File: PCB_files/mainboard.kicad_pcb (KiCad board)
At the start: 2 copper layers, 45 parts, among them J1 Conn_01x01_Male, J2 Conn_01x01_Male, J3 Conn_01x01_Male, J4 Conn_01x20, J5 Conn_01x20, J6 Conn_01x06_Male, U1 IFX007TAUMA1, U2 IFX007TAUMA1, U3 IFX007TAUMA1, U4 LM2931-5.0_SO8

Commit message: Started routing components
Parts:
- C1, C2, C3, C4, C5, C6: footprint Capacitor_SMD:C_0805_2012Metric -> Capacitor_SMD:C_0603_1608Metric_Pad1.05x0.95mm_HandSolder; moved to B.Cu
- C14, C15: moved to B.Cu
- R1, R2, R3, R4, R5, R6, R9: footprint Resistor_SMD:R_0805_2012Metric -> Resistor_SMD:R_0603_1608Metric_Pad1.05x0.95mm_HandSolder; moved to B.Cu
- R10, R11, R12, R13, R14, R7, R8: footprint Resistor_SMD:R_0805_2012Metric -> Resistor_SMD:R_0603_1608Metric_Pad1.05x0.95mm_HandSolder
- moved R9 67.4 mm to (192.3, 94.1), turned to 270 degrees
- moved C2 67.2 mm to (178.9, 76.1), turned to 180 degrees
- moved C7 64.1 mm to (198.1, 93.4), turned to 180 degrees
- moved C8 59.4 mm to (198.5, 107.1)
- moved C11 58.2 mm to (187.7, 94.1), turned to 90 degrees
- moved R2 49.0 mm to (177.2, 80.2), turned to 180 degrees
- moved C12 47.4 mm to (188.7, 105.4), turned to 180 degrees
- moved C4 47.2 mm to (168.0, 99.1), turned to 90 degrees
- moved R5 46.9 mm to (143.8, 99.9), turned to 90 degrees
- moved C16 46.2 mm to (189.2, 101.9), turned to 90 degrees
- moved C14 42.5 mm to (162.3, 96.4), turned to 90 degrees
- moved R6 37.0 mm to (140.8, 101.2), turned to 90 degrees
- moved C3 35.8 mm to (162.9, 99.9), turned to 90 degrees
- moved C9 32.5 mm to (137.9, 96.1), turned to 90 degrees
- moved R4 31.5 mm to (170.4, 99.1), turned to 90 degrees
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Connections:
- net Net-(C1-Pad1) renamed /sr1
- net Net-(C3-Pad1) renamed /sr2
- net Net-(C5-Pad1) renamed /sr3
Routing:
- net GND: track 107.8 -> 163.3 mm, vias 0 -> 3
- net +BATT: track 96.4 -> 129.7 mm, vias 0 -> 1
- net Net-(C2-Pad1): track 0.00 -> 30.8 mm, vias 0 -> 2
- net Net-(C7-Pad1): track 0.00 -> 28.2 mm
- net Net-(J4-Pad5): track 0.00 -> 27.6 mm, vias 0 -> 1
- net Net-(C11-Pad1): track 0.00 -> 25.7 mm
- net Net-(C14-Pad1): track 0.00 -> 22.8 mm, vias 0 -> 1
- net /sr1: track 0.00 -> 14.8 mm, vias 0 -> 1
- net Net-(C6-Pad1): track 0.00 -> 8.27 mm, vias 0 -> 1
- net Net-(R9-Pad2): track 0.00 -> 8.05 mm, vias 0 -> 1
- net Net-(C4-Pad1): track 0.00 -> 7.55 mm, vias 0 -> 1
- net /sr3: track 0.00 -> 5.66 mm, vias 0 -> 1
- net /sr2: track 0.00 -> 4.84 mm, vias 0 -> 1

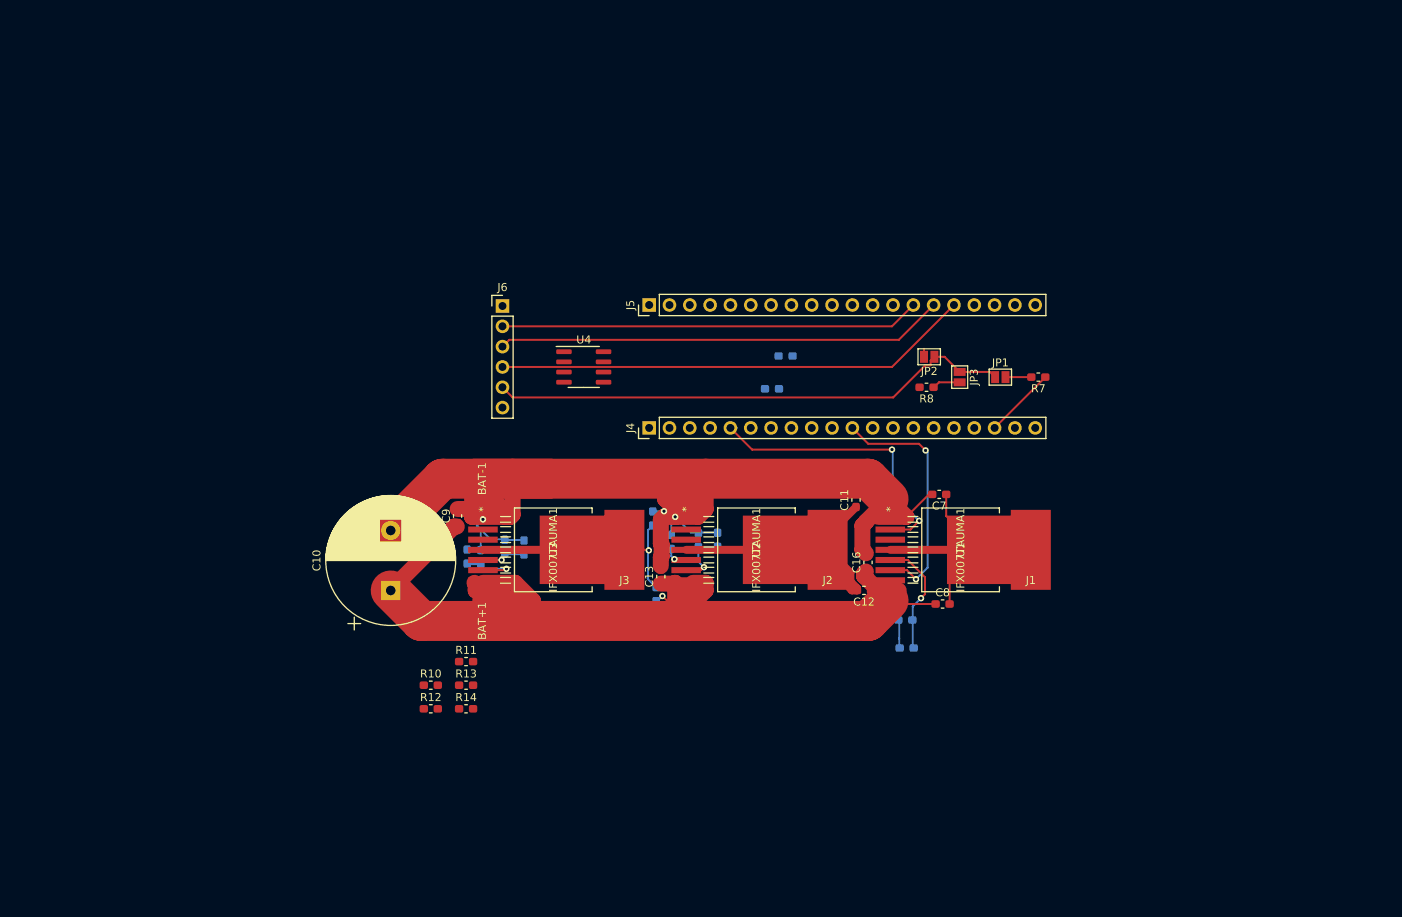
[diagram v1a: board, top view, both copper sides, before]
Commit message: Finished routing and added footprint file for driver chip
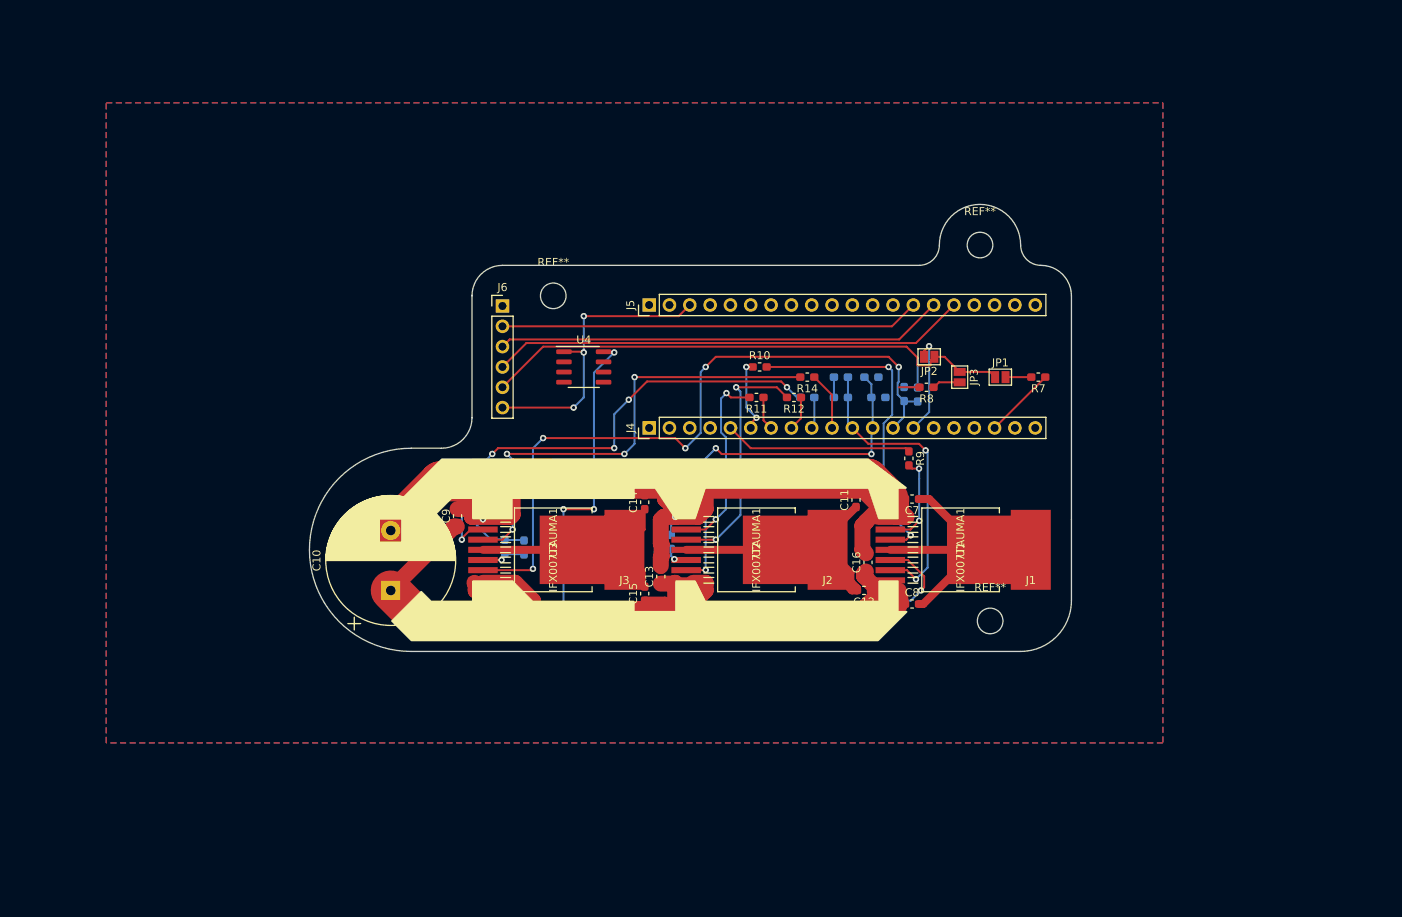
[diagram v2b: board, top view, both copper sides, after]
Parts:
- added REF**: MountingHole_3.2mm_M3, MountingHole:MountingHole_3.2mm_M3, F.Cu at (203.2, 62.2)
- added REF**: MountingHole_3.2mm_M3, MountingHole:MountingHole_3.2mm_M3, F.Cu at (149.9, 68.6)
- added REF**: MountingHole_3.2mm_M3, MountingHole:MountingHole_3.2mm_M3, F.Cu at (204.5, 109.2)
- C14, C15, R9: moved to F.Cu
- R13: moved to B.Cu
- moved R12 59.8 mm to (179.9, 81.3), turned to 180 degrees
- moved R14 59.5 mm to (181.6, 78.7), turned to 180 degrees
- moved C6 58.3 mm to (193.7, 80.9)
- moved R6 58.3 mm to (195.4, 80.9)
- moved R10 57.2 mm to (175.7, 77.5)
- moved R13 55.8 mm to (181.6, 81.3), turned to 180 degrees
- moved R11 49.1 mm to (175.3, 81.3), turned to 180 degrees
- moved C4 29.7 mm to (189.6, 78.7), turned to 0 degrees
- moved R4 26.8 mm to (190.5, 81.3), turned to 0 degrees
- moved R2 8.68 mm to (185.8, 81.3)
- moved C2 7.40 mm to (185.8, 78.7)
- moved R9 5.57 mm to (194.3, 88.9)
- moved R1 5.56 mm to (189.6, 109.2)
- moved C8 3.82 mm to (194.7, 107.1)
- moved C7 3.44 mm to (194.7, 94.0)
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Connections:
- J5 pad 1: +3V3 -> Net-(J5-Pad1)
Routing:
- net Net-(C6-Pad1): track 8.27 -> 88.2 mm, vias 1 -> 5
- net Net-(R13-Pad2): track 0.00 -> 61.1 mm, vias 0 -> 5
- net Net-(R14-Pad2): track 0.00 -> 59.5 mm, vias 0 -> 4
- net Net-(C4-Pad1): track 7.55 -> 49.9 mm, vias 1 -> 3
- net +BATT: track 129.7 -> 171.1 mm, vias 1 -> 4
- net Net-(R10-Pad2): track 0.00 -> 41.1 mm, vias 0 -> 2
- net VCC: track 0.00 -> 37.2 mm, vias 0 -> 3
- net Net-(R12-Pad2): track 0.00 -> 31.1 mm, vias 0 -> 2
- net Net-(R11-Pad2): track 0.00 -> 24.2 mm, vias 0 -> 2
- net Net-(C7-Pad1): track 28.2 -> 43.6 mm
- net Net-(J4-Pad14): track 1.00 -> 12.6 mm, vias 0 -> 1
- net Net-(J4-Pad6): track 0.00 -> 9.23 mm, vias 0 -> 2
- net Net-(J4-Pad10): track 0.00 -> 7.27 mm
- net Net-(C14-Pad1): track 22.8 -> 29.5 mm, vias 1 -> 0
- net Net-(C2-Pad1): track 30.8 -> 37.4 mm
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- added copper zone on B.Cu, net GND
- added copper zone on F.Cu, net GND
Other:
- board outline added: 95.2 x 55.9 mm

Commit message: fixed half-bridge driver footprints
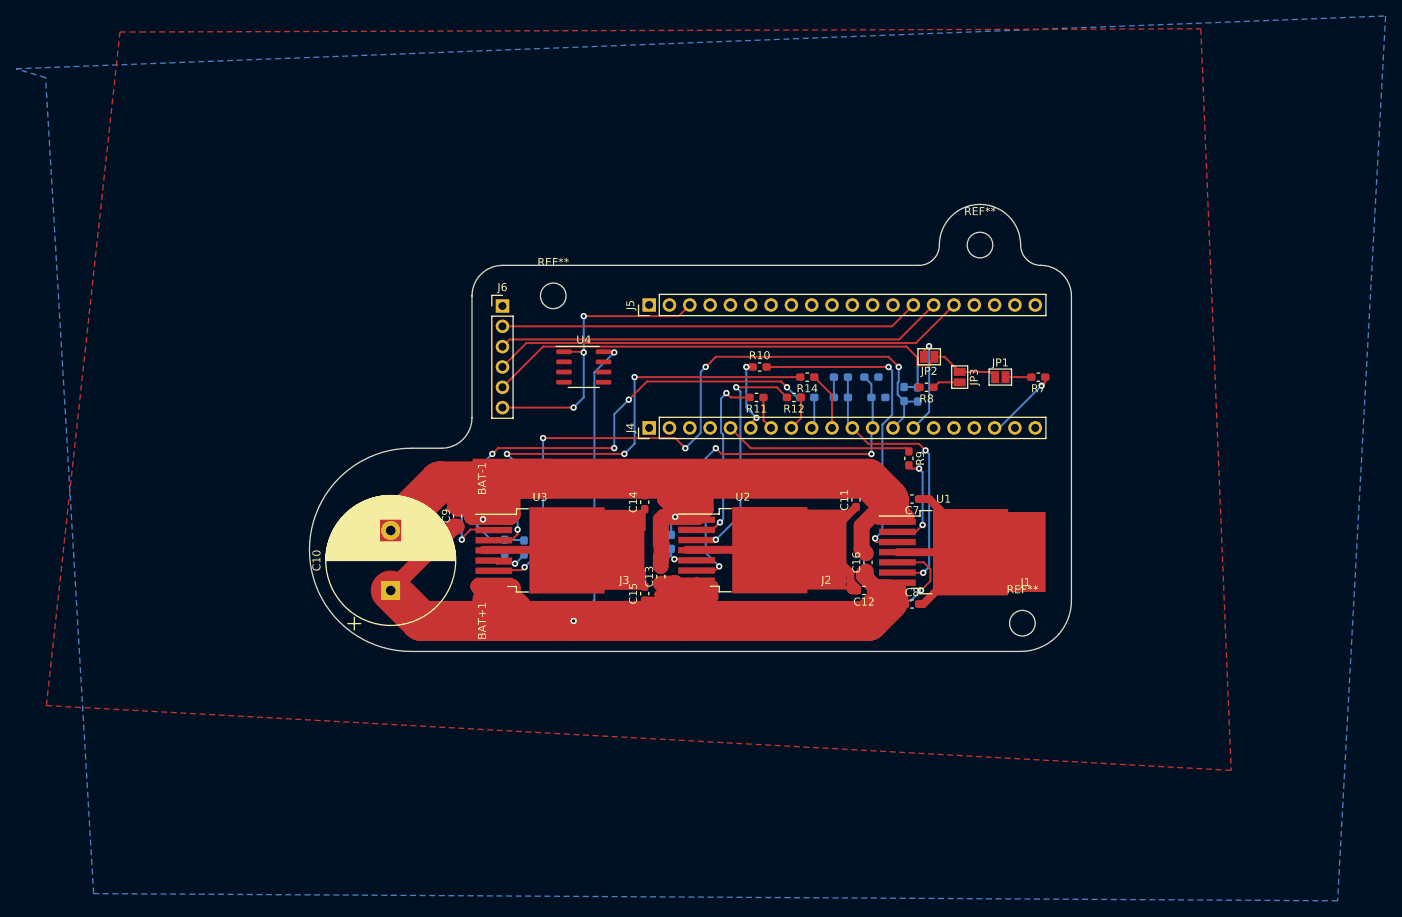
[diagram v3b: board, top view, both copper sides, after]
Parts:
- U1, U2, U3: footprint 2020-09-26_17-28-12:IFX007TAUMA1 -> Package_TO_SOT_SMD:TO-263-7_TabPin8
- moved REF** 4.04 mm to (208.5, 109.5)
- moved U1 2.14 mm to (198.7, 100.6), turned to 0 degrees
- moved U2 1.71 mm to (173.6, 100.4), turned to 0 degrees
- moved U3 1.66 mm to (148.2, 100.4), turned to 0 degrees
- moved J1 0.70 mm to (208.9, 100.6)
- moved J2 0.15 mm to (184.0, 100.3)
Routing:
- net GND: track 156.7 -> 160.5 mm
- net Net-(C4-Pad1): track 49.9 -> 47.8 mm
- net Net-(C7-Pad1): track 43.6 -> 41.5 mm
- net Net-(C2-Pad1): track 37.4 -> 35.9 mm
- net /sr3: track 5.66 -> 4.38 mm
- net /sr1: track 13.9 -> 15.1 mm
- net Net-(R14-Pad2): track 59.5 -> 60.7 mm
- net Net-(C6-Pad1): track 88.2 -> 87.5 mm
- net +3V3: track 9.03 -> 9.37 mm, vias 0 -> 1
- net +BATT: track 171.1 -> 171.4 mm, vias 4 -> 2

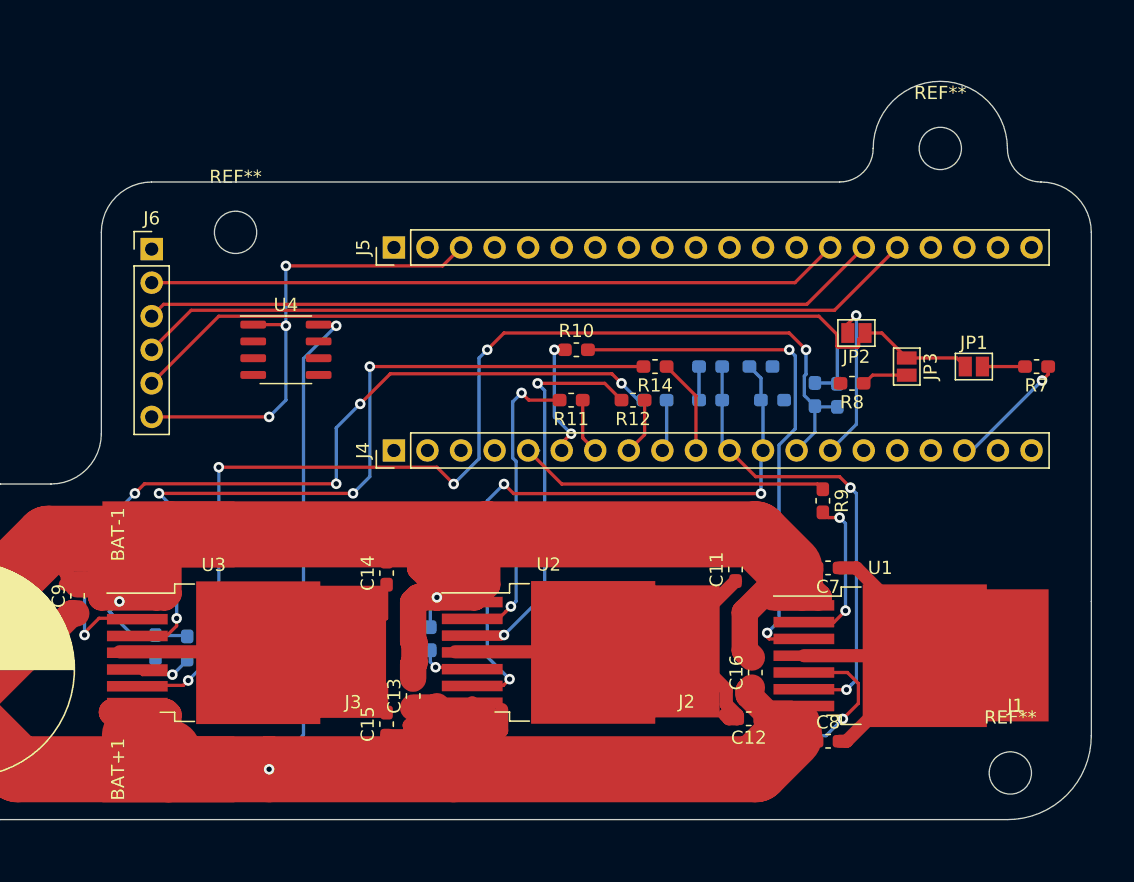
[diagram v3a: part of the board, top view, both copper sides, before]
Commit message: Optimized ground planes and added thermal vias to half-bridges
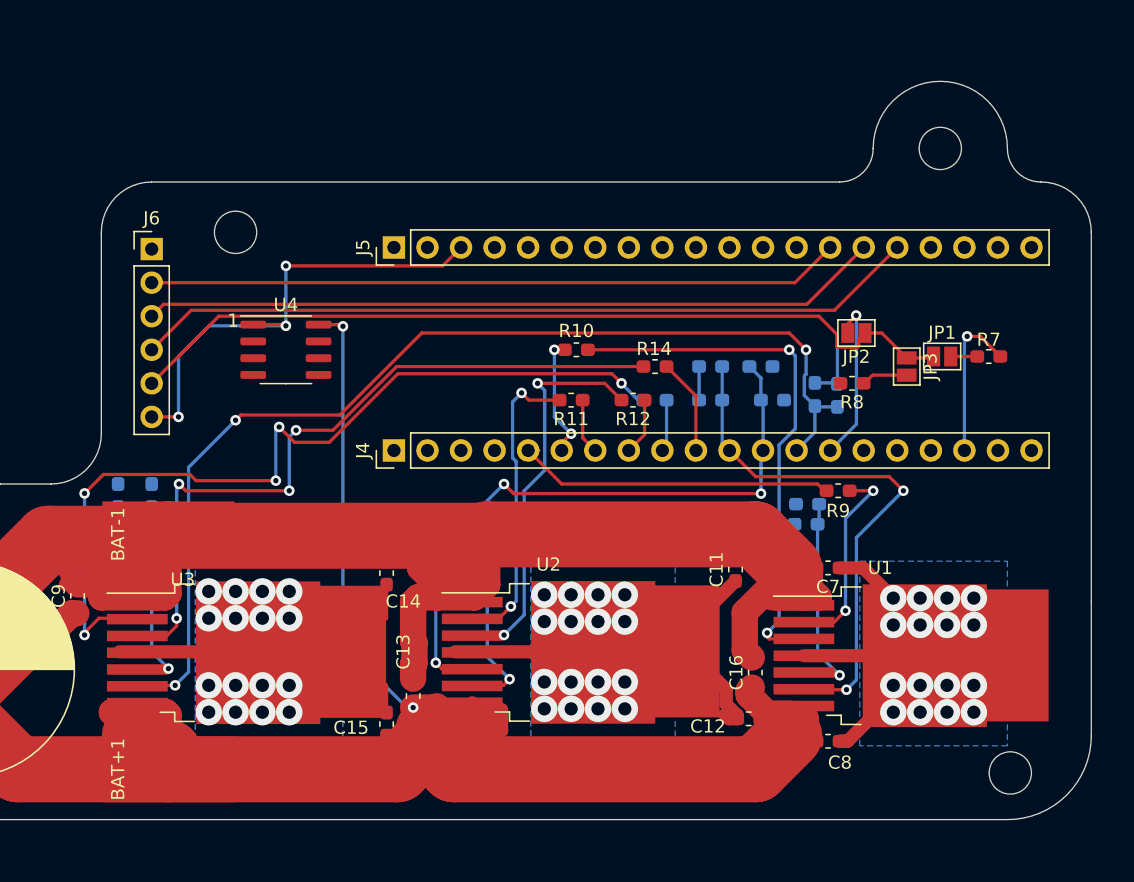
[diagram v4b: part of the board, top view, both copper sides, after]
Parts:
- moved R1 20.4 mm to (193.2, 89.2)
- moved C1 16.0 mm to (193.0, 90.7)
- moved C5 11.8 mm to (143.5, 88.5)
- moved R5 11.8 mm to (141.0, 88.5)
- moved C3 9.71 mm to (166.9, 91.0)
- moved R3 8.27 mm to (164.8, 91.1)
- moved R7 3.70 mm to (206.9, 78.0)
- moved JP1 2.52 mm to (203.3, 78.0)
- moved R9 1.39 mm to (195.5, 88.1), turned to 0 degrees
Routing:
- net /sr3: track 4.38 -> 17.7 mm
- net GND: track 160.5 -> 148.0 mm, vias 2 -> 0
- net Net-(C7-Pad1): track 41.5 -> 30.9 mm, vias 0 -> 16
- net /sr2: track 4.84 -> 14.3 mm
- net Net-(C2-Pad1): track 35.9 -> 41.1 mm
- net Net-(C6-Pad1): track 87.5 -> 82.9 mm, vias 5 -> 3
- net Net-(R14-Pad2): track 60.7 -> 57.1 mm
- net Net-(R13-Pad2): track 61.1 -> 64.5 mm
- net Net-(R9-Pad2): track 12.2 -> 15.2 mm
- net Net-(J6-Pad5): track 67.0 -> 64.4 mm
- net +3V3: track 9.37 -> 11.9 mm
- net /sr1: track 15.1 -> 16.5 mm
- net Net-(JP1-Pad2): track 3.16 -> 2.00 mm
- net VCC: track 37.2 -> 36.6 mm
- net Net-(C14-Pad1): vias 0 -> 16
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- added copper zone on B.Cu, net Net-(C11-Pad1)
- added copper zone on B.Cu, net Net-(C14-Pad1)
- added copper zone on B.Cu, net Net-(C7-Pad1)
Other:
- board text added: "1"

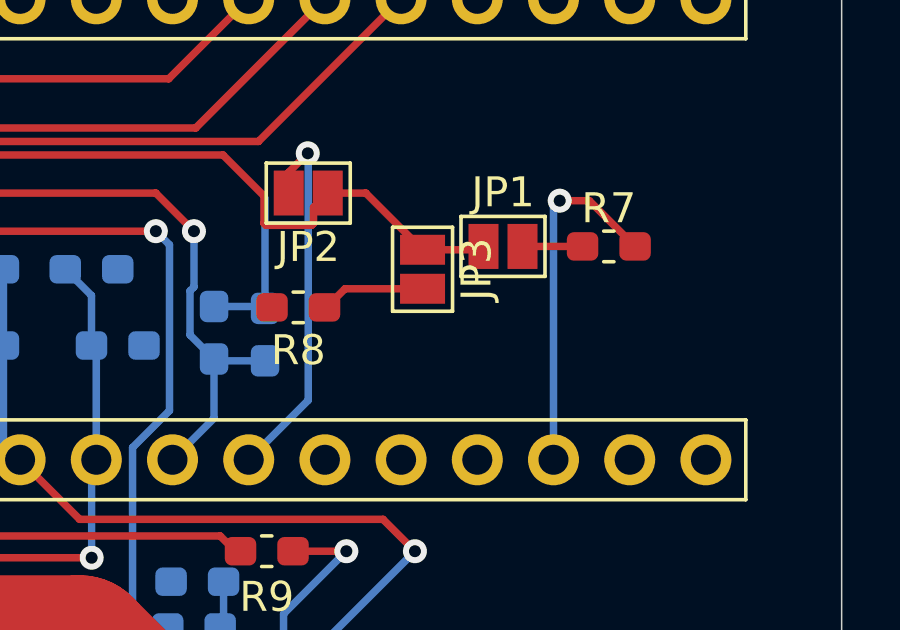
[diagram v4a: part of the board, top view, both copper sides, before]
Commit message: Optimized routing and schematic clarity
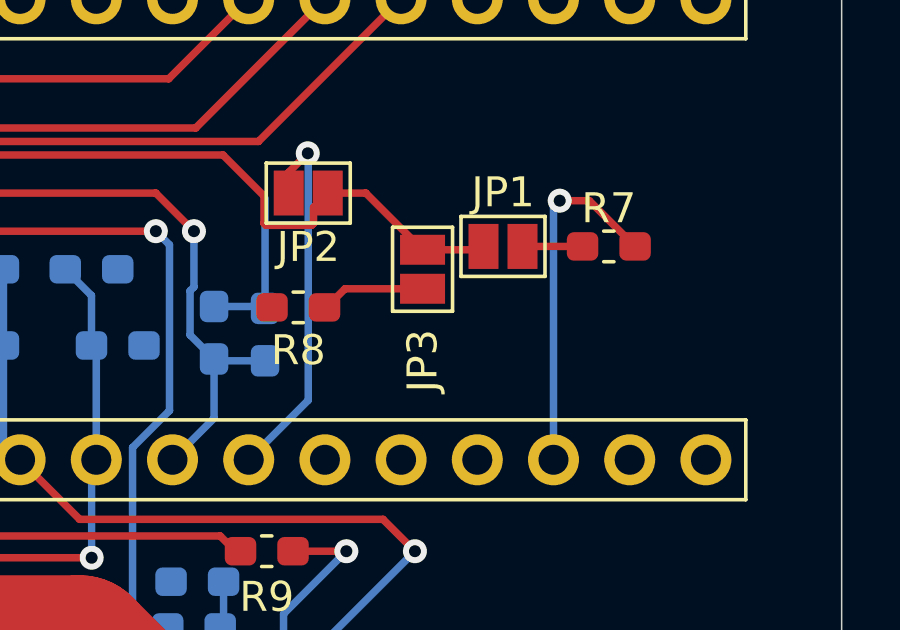
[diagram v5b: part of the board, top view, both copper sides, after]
